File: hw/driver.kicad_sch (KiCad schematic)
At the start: 28 parts, among them Q301 CSD17571Q2, U1 UCC27511DBVR, U201 NCV8460A, U303 INA2180A2IDGKR

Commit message: Fixed some bugs
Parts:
- C327: value 47uF -> 22uF 100V; LCSC C342293 -> C575373
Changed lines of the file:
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@@
       (effects (font (size 1.27 1.27)) (justify left))
     )
-    (property "Value" "47uF" (at 127 59.055 0)
+    (property "Value" "22uF 100V" (at 127 59.055 0)
       (effects (font (size 1.27 1.27)) (justify left))
     )
@@
       (effects (font (size 1.27 1.27)) hide)
     )
-    (property "LCSC" "C342293" (at 125.73 56.515 0)
+    (property "LCSC" "C575373" (at 125.73 56.515 0)
       (effects (font (size 1.27 1.27)) hide)
     )

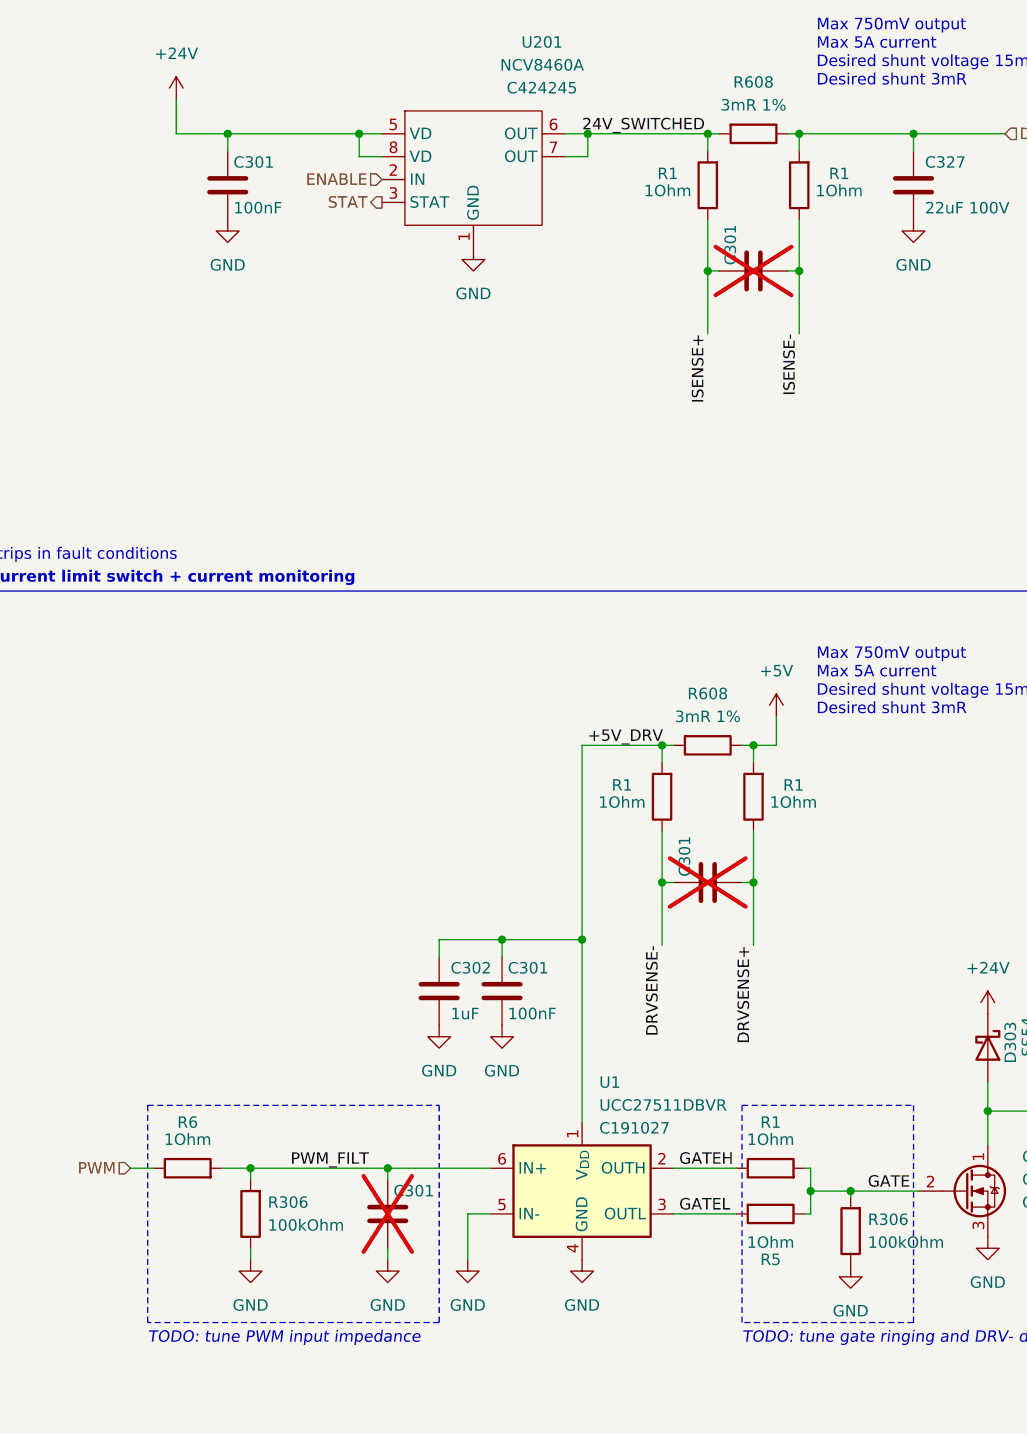
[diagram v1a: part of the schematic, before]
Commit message: Removed R{1,2}02 pull-down because it ruins strap
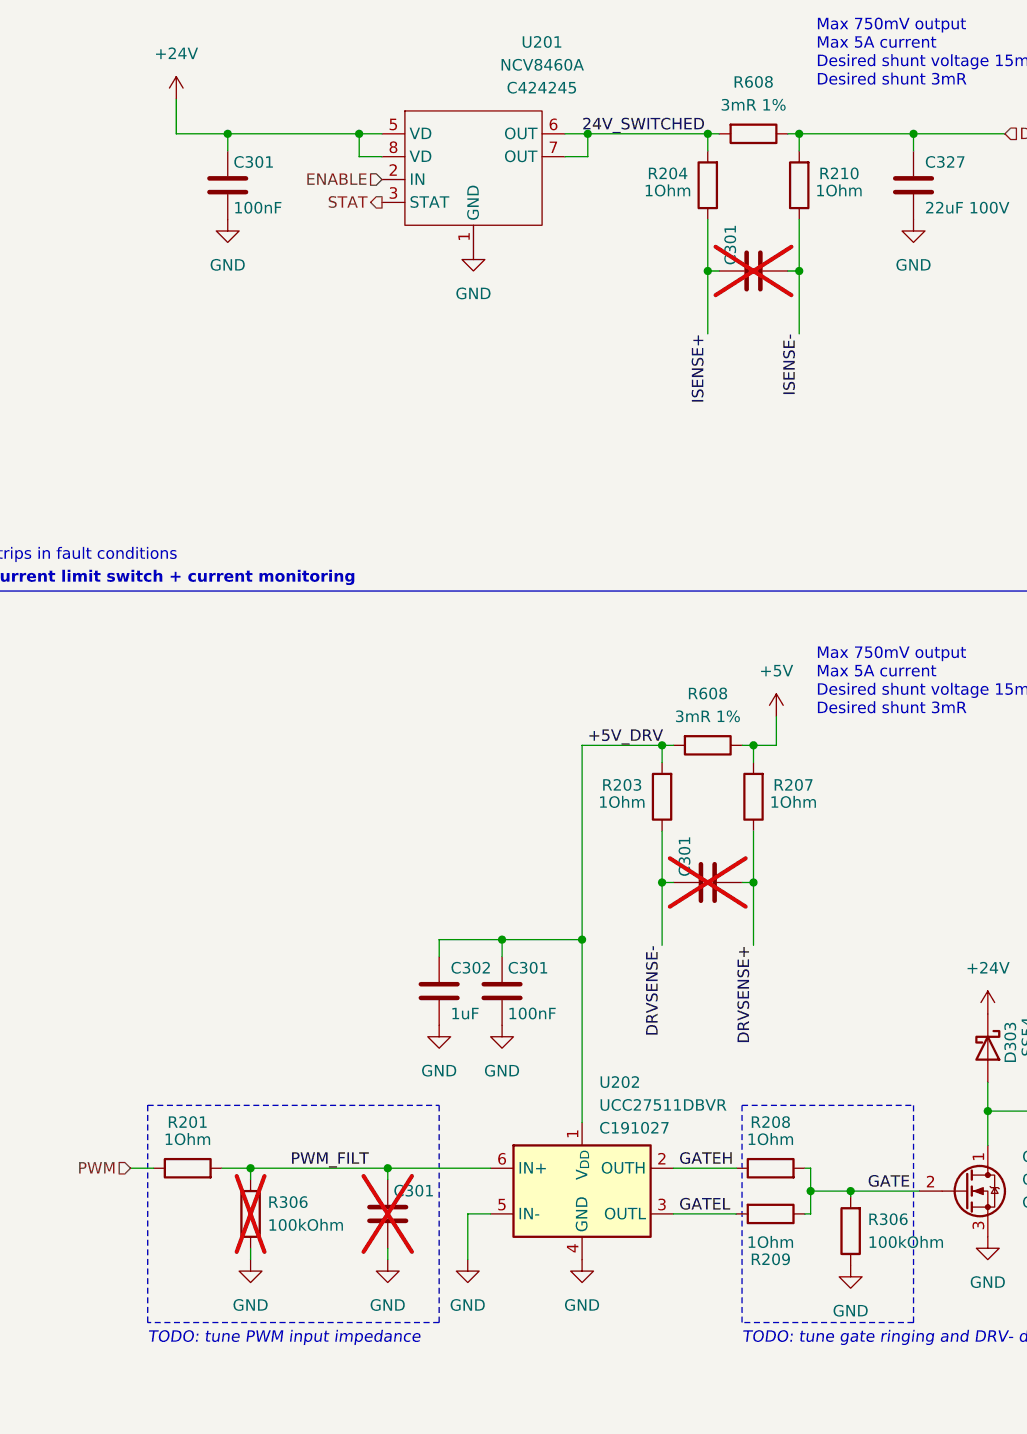
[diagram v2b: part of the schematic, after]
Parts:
- R306: now not fitted; now left out of the parts list
- renumbered R6 to R201, R1 to R203, R1 to R204, R1 to R207, R1 to R208, R5 to R209, R1 to R210, U1 to U202
